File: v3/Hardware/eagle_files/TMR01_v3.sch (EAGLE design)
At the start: 28 parts, among them IC1 DS3231/SO, U1 ATMEGA328P_TQFP

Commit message: fixed sda scl in rtc
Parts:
- added TP3, TP4: TEST-POINT3X4, SparkFun-Connectors:TEST-POINT3X4
- S1: value MOMENTARY-SWITCH-SPST-SMD-5.2MM -> MOMENTARY-SWITCH-SPST; device SparkFun-Switches:MOMENTARY-SWITCH-SPST-SMD-5.2MM -> SparkFun-Switches:MOMENTARY-SWITCH-SPST
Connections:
- net RX: now also TP3.1
- net SCL: now also IC1.SCL, R2.1; no longer IC1.SDA, R3.1
- net SDA: now also IC1.SDA, R3.1; no longer IC1.SCL, R2.1
- net TX: now also TP4.1
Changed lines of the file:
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@@
 <part name="C1" library="Perfect_0402" deviceset="CAP_0402" device="" value="100nF"/>
 <part name="R5" library="Perfect_0402" deviceset="RES_0402" device="" value="10k"/>
-<part name="S1" library="SparkFun-Switches" deviceset="MOMENTARY-SWITCH-SPST" device="-SMD-5.2MM"/>
+<part name="S1" library="SparkFun-Switches" deviceset="MOMENTARY-SWITCH-SPST" device=""/>
+<part name="TP3" library="SparkFun-Connectors" deviceset="TEST-POINT" device="3X4"/>
+<part name="TP4" library="SparkFun-Connectors" deviceset="TEST-POINT" device="3X4"/>
 </parts>
 <sheets>
@@
 <instance part="S1" gate="G$1" x="83.82" y="124.46" smashed="yes">
 <attribute name="NAME" x="83.82" y="125.984" size="1.778" layer="95" font="vector" align="bottom-center"/>
+</instance>
+<instance part="TP3" gate="G$1" x="104.14" y="149.86" smashed="yes" rot="R180">
+<attribute name="NAME" x="106.68" y="149.86" size="1.778" layer="95" font="vector" rot="R180"/>
+</instance>
+<instance part="TP4" gate="G$1" x="104.14" y="144.78" smashed="yes" rot="R180">
+<attribute name="NAME" x="106.68" y="144.78" size="1.778" layer="95" font="vector" rot="R180"/>
 </instance>
 </instances>
@@
 <label x="182.88" y="139.7" size="1.778" layer="95"/>
 </segment>
+<segment>
+<wire x1="104.14" y1="149.86" x2="111.76" y2="149.86" width="0.1524" layer="91"/>
+<label x="109.22" y="149.86" size="1.778" layer="95"/>
+<pinref part="TP3" gate="G$1" pin="1"/>
+</segment>
 </net>
 <net name="TX" class="0">
@@
 <wire x1="177.8" y1="137.16" x2="185.42" y2="137.16" width="0.1524" layer="91"/>
 <label x="182.88" y="137.16" size="1.778" layer="95"/>
+</segment>
+<segment>
+<wire x1="104.14" y1="144.78" x2="111.76" y2="144.78" width="0.1524" layer="91"/>
+<label x="109.22" y="144.78" size="1.778" layer="95"/>
+<pinref part="TP4" gate="G$1" pin="1"/>
 </segment>
 </net>
@@
 </segment>
 <segment>
+<wire x1="170.18" y1="71.12" x2="187.96" y2="71.12" width="0.1524" layer="91"/>
+<wire x1="187.96" y1="71.12" x2="187.96" y2="78.74" width="0.1524" layer="91"/>
+<label x="172.72" y="71.12" size="1.778" layer="95"/>
+<pinref part="IC1" gate="G$1" pin="SDA"/>
+<pinref part="R3" gate="G$1" pin="1"/>
+</segment>
+</net>
+<net name="SCL" class="0">
+<segment>
+<pinref part="U1" gate="U1" pin="PC5(ADC5/SCL)"/>
+<wire x1="177.8" y1="149.86" x2="185.42" y2="149.86" width="0.1524" layer="91"/>
+<label x="182.88" y="149.86" size="1.778" layer="95"/>
+</segment>
+<segment>
 <pinref part="IC1" gate="G$1" pin="SCL"/>
 <wire x1="170.18" y1="73.66" x2="180.34" y2="73.66" width="0.1524" layer="91"/>
@@
 </segment>
 </net>
-<net name="SCL" class="0">
-<segment>
-<wire x1="170.18" y1="71.12" x2="187.96" y2="71.12" width="0.1524" layer="91"/>
-<wire x1="187.96" y1="71.12" x2="187.96" y2="78.74" width="0.1524" layer="91"/>
-<label x="172.72" y="71.12" size="1.778" layer="95"/>
-<pinref part="IC1" gate="G$1" pin="SDA"/>
-<pinref part="R3" gate="G$1" pin="1"/>
-</segment>
-<segment>
-<pinref part="U1" gate="U1" pin="PC5(ADC5/SCL)"/>
-<wire x1="177.8" y1="149.86" x2="185.42" y2="149.86" width="0.1524" layer="91"/>
-<label x="182.88" y="149.86" size="1.778" layer="95"/>
-</segment>
-</net>

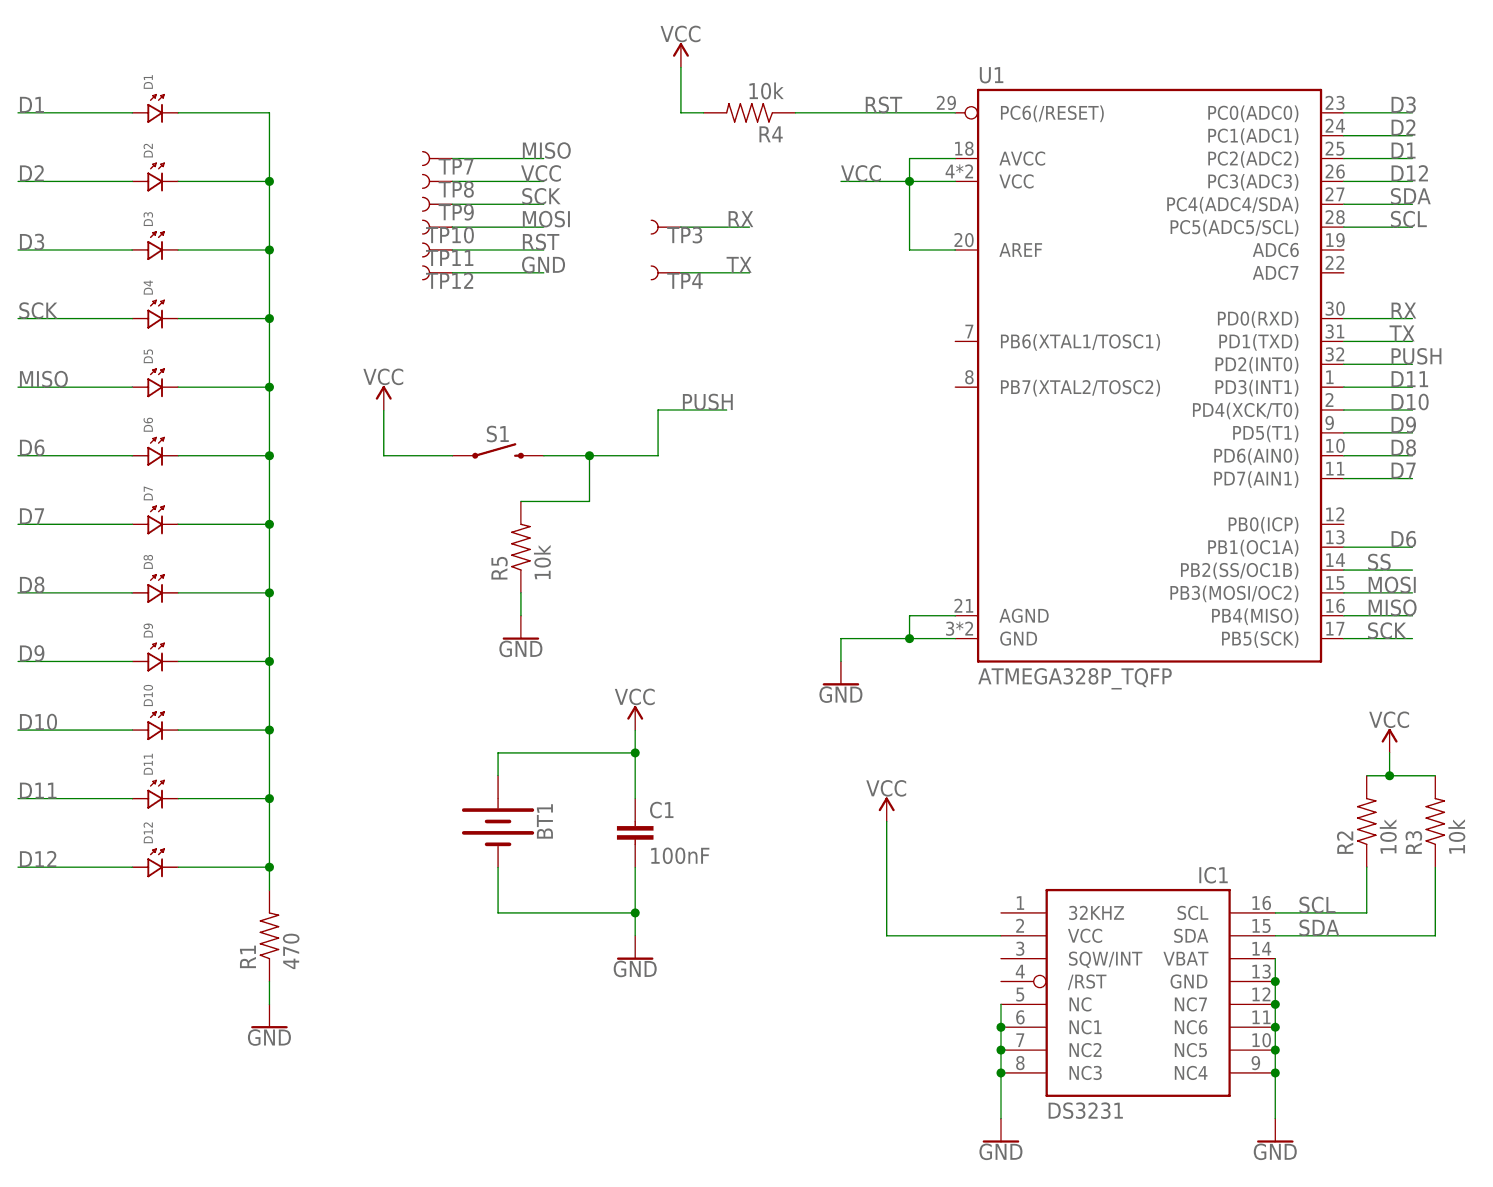
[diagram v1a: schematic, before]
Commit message: pins output modified, not using miso mosi connected to leds
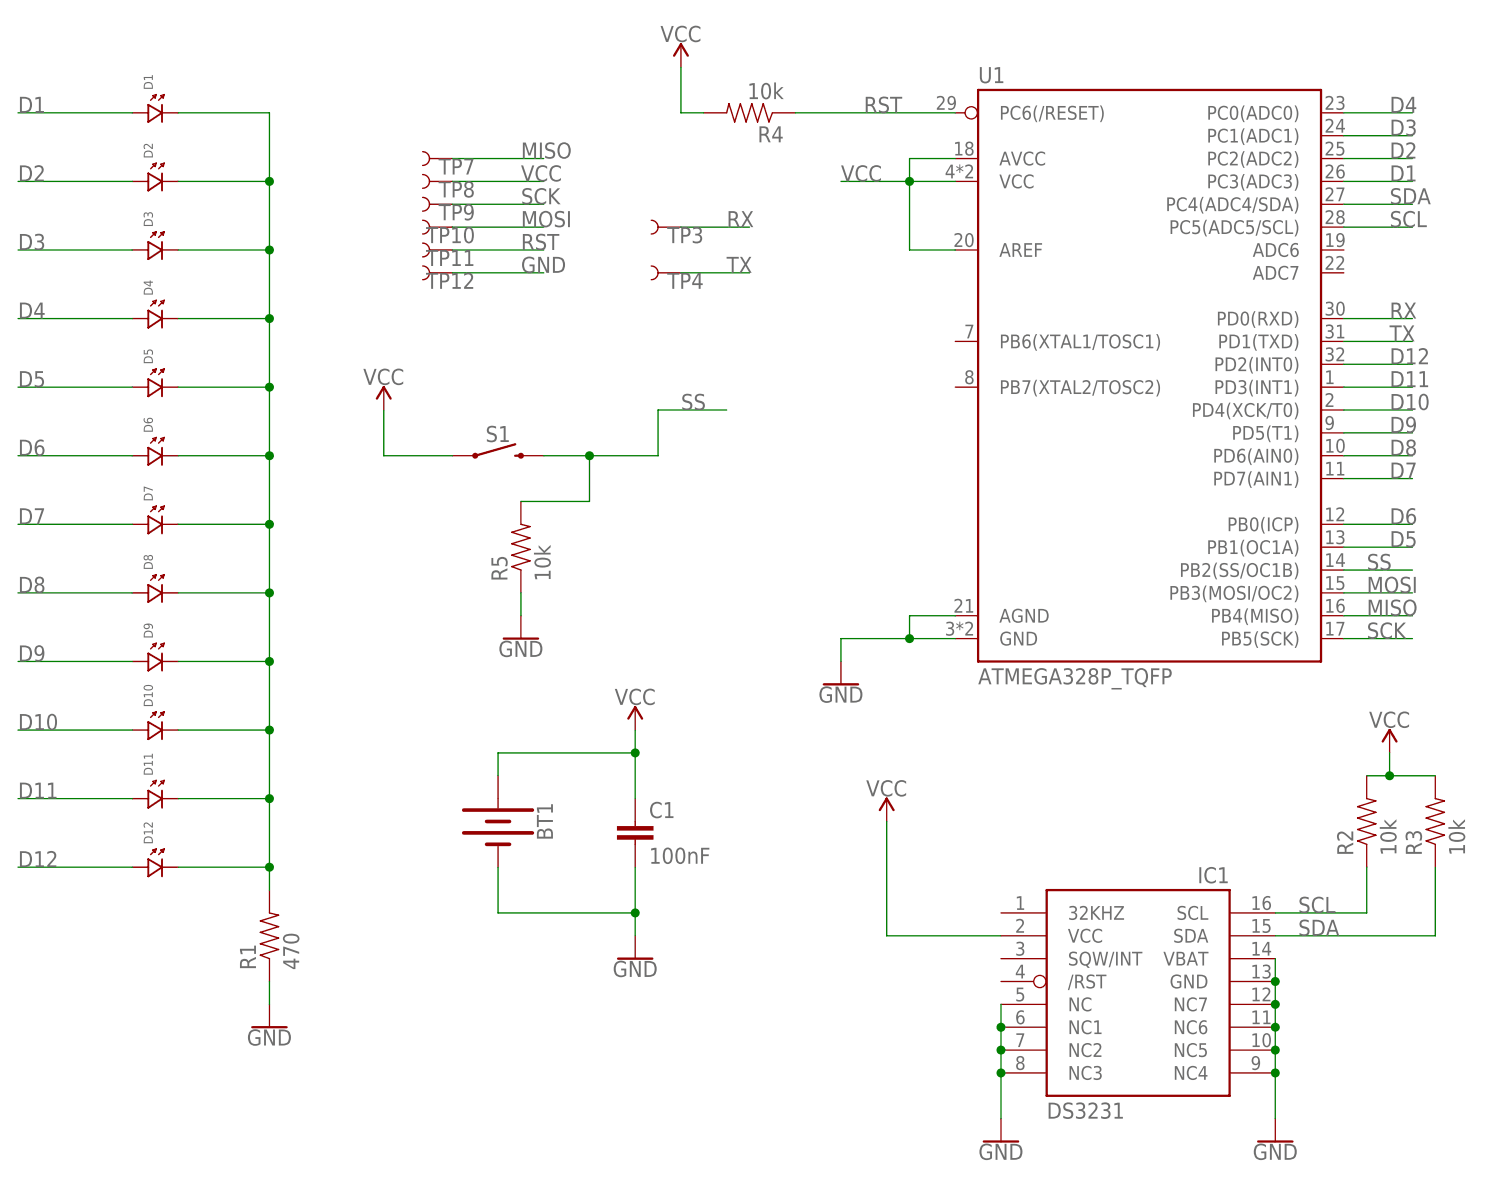
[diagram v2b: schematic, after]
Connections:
- removed net PUSH: R5.2, S1.2, U1.PD2(INT0)
- new net D4: D4.1, U1.PC0(ADC0)
- new net D5: D5.1, U1.PB1(OC1A)
- net D1: now also U1.PC3(ADC3); no longer U1.PC2(ADC2)
- net D12: now also U1.PD2(INT0); no longer U1.PC3(ADC3)
- net D2: now also U1.PC2(ADC2); no longer U1.PC1(ADC1)
- net D3: now also U1.PC1(ADC1); no longer U1.PC0(ADC0)
- net D6: now also U1.PB0(ICP); no longer U1.PB1(OC1A)
- net MISO: no longer D5.1
- net SCK: no longer D4.1
- net SS: now also R5.2, S1.2
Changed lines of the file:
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@@
 <pinref part="TP7" gate="G$1" pin="1"/>
-</segment>
-<segment>
-<wire x1="43.18" y1="132.08" x2="30.48" y2="132.08" width="0.1524" layer="91"/>
-<label x="30.48" y="132.08" size="1.778" layer="95"/>
-<pinref part="D5" gate="G$1" pin="1"/>
 </segment>
 </net>
@@
 <pinref part="TP9" gate="G$1" pin="1"/>
 </segment>
-<segment>
-<wire x1="43.18" y1="139.7" x2="30.48" y2="139.7" width="0.1524" layer="91"/>
-<label x="30.48" y="139.7" size="1.778" layer="95"/>
-<pinref part="D4" gate="G$1" pin="1"/>
-</segment>
 </net>
 <net name="D1" class="0">
@@
 </segment>
 <segment>
+<pinref part="U1" gate="U1" pin="PC3(ADC3)"/>
+<wire x1="177.8" y1="154.94" x2="185.42" y2="154.94" width="0.1524" layer="91"/>
+<label x="182.88" y="154.94" size="1.778" layer="95"/>
+</segment>
+</net>
+<net name="D2" class="0">
+<segment>
+<wire x1="43.18" y1="154.94" x2="30.48" y2="154.94" width="0.1524" layer="91"/>
+<label x="30.48" y="154.94" size="1.778" layer="95"/>
+<pinref part="D2" gate="G$1" pin="1"/>
+</segment>
+<segment>
 <pinref part="U1" gate="U1" pin="PC2(ADC2)"/>
 <wire x1="177.8" y1="157.48" x2="185.42" y2="157.48" width="0.1524" layer="91"/>
@@
 </segment>
 </net>
-<net name="D2" class="0">
-<segment>
-<wire x1="43.18" y1="154.94" x2="30.48" y2="154.94" width="0.1524" layer="91"/>
-<label x="30.48" y="154.94" size="1.778" layer="95"/>
-<pinref part="D2" gate="G$1" pin="1"/>
+<net name="D3" class="0">
+<segment>
+<wire x1="43.18" y1="147.32" x2="30.48" y2="147.32" width="0.1524" layer="91"/>
+<label x="30.48" y="147.32" size="1.778" layer="95"/>
+<pinref part="D3" gate="G$1" pin="1"/>
 </segment>
 <segment>
@@
 </segment>
 </net>
-<net name="D3" class="0">
-<segment>
-<wire x1="43.18" y1="147.32" x2="30.48" y2="147.32" width="0.1524" layer="91"/>
-<label x="30.48" y="147.32" size="1.778" layer="95"/>
-<pinref part="D3" gate="G$1" pin="1"/>
-</segment>
-<segment>
-<pinref part="U1" gate="U1" pin="PC0(ADC0)"/>
-<wire x1="177.8" y1="162.56" x2="185.42" y2="162.56" width="0.1524" layer="91"/>
-<label x="182.88" y="162.56" size="1.778" layer="95"/>
-</segment>
-</net>
 <net name="D6" class="0">
 <segment>
@@
 </segment>
 <segment>
-<pinref part="U1" gate="U1" pin="PB1(OC1A)"/>
-<wire x1="177.8" y1="114.3" x2="185.42" y2="114.3" width="0.1524" layer="91"/>
-<label x="182.88" y="114.3" size="1.778" layer="95"/>
-</segment>
-</net>
-<net name="PUSH" class="0">
+<pinref part="U1" gate="U1" pin="PB0(ICP)"/>
+<wire x1="177.8" y1="116.84" x2="185.42" y2="116.84" width="0.1524" layer="91"/>
+<label x="182.88" y="116.84" size="1.778" layer="95"/>
+</segment>
+</net>
+<net name="SS" class="0">
+<segment>
+<pinref part="U1" gate="U1" pin="PB2(SS/OC1B)"/>
+<wire x1="177.8" y1="111.76" x2="185.42" y2="111.76" width="0.1524" layer="91"/>
+<label x="180.34" y="111.76" size="1.778" layer="95"/>
+</segment>
 <segment>
 <wire x1="88.9" y1="124.46" x2="93.98" y2="124.46" width="0.1524" layer="91"/>
@@
 <pinref part="S1" gate="G$1" pin="2"/>
 </segment>
+</net>
+<net name="D12" class="0">
+<segment>
+<wire x1="43.18" y1="78.74" x2="30.48" y2="78.74" width="0.1524" layer="91"/>
+<label x="30.48" y="78.74" size="1.778" layer="95"/>
+<pinref part="D12" gate="G$1" pin="1"/>
+</segment>
 <segment>
 <pinref part="U1" gate="U1" pin="PD2(INT0)"/>
 <wire x1="177.8" y1="134.62" x2="185.42" y2="134.62" width="0.1524" layer="91"/>
 <label x="182.88" y="134.62" size="1.778" layer="95"/>
-</segment>
-</net>
-<net name="SS" class="0">
-<segment>
-<pinref part="U1" gate="U1" pin="PB2(SS/OC1B)"/>
-<wire x1="177.8" y1="111.76" x2="185.42" y2="111.76" width="0.1524" layer="91"/>
-<label x="180.34" y="111.76" size="1.778" layer="95"/>
-</segment>
-</net>
-<net name="D12" class="0">
-<segment>
-<pinref part="U1" gate="U1" pin="PC3(ADC3)"/>
-<wire x1="177.8" y1="154.94" x2="185.42" y2="154.94" width="0.1524" layer="91"/>
-<label x="182.88" y="154.94" size="1.778" layer="95"/>
-</segment>
-<segment>
-<wire x1="43.18" y1="78.74" x2="30.48" y2="78.74" width="0.1524" layer="91"/>
-<label x="30.48" y="78.74" size="1.778" layer="95"/>
-<pinref part="D12" gate="G$1" pin="1"/>
 </segment>
 </net>
@@
 </segment>
 </net>
+<net name="D5" class="0">
+<segment>
+<pinref part="U1" gate="U1" pin="PB1(OC1A)"/>
+<wire x1="177.8" y1="114.3" x2="185.42" y2="114.3" width="0.1524" layer="91"/>
+<label x="182.88" y="114.3" size="1.778" layer="95"/>
+</segment>
+<segment>
+<wire x1="43.18" y1="132.08" x2="30.48" y2="132.08" width="0.1524" layer="91"/>
+<label x="30.48" y="132.08" size="1.778" layer="95"/>
+<pinref part="D5" gate="G$1" pin="1"/>
+</segment>
+</net>
+<net name="D4" class="0">
+<segment>
+<pinref part="U1" gate="U1" pin="PC0(ADC0)"/>
+<wire x1="177.8" y1="162.56" x2="185.42" y2="162.56" width="0.1524" layer="91"/>
+<label x="182.88" y="162.56" size="1.778" layer="95"/>
+</segment>
+<segment>
+<wire x1="43.18" y1="139.7" x2="30.48" y2="139.7" width="0.1524" layer="91"/>
+<label x="30.48" y="139.7" size="1.778" layer="95"/>
+<pinref part="D4" gate="G$1" pin="1"/>
+</segment>
+</net>

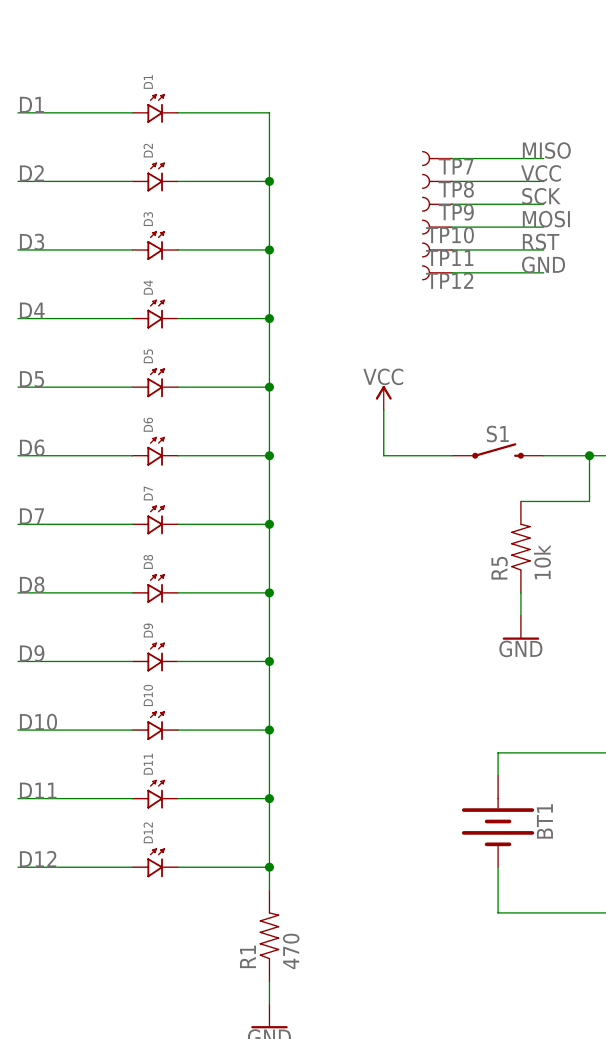
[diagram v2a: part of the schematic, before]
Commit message: 0402 leds possible wrong footprint. Changed temporaly by resistors footprint
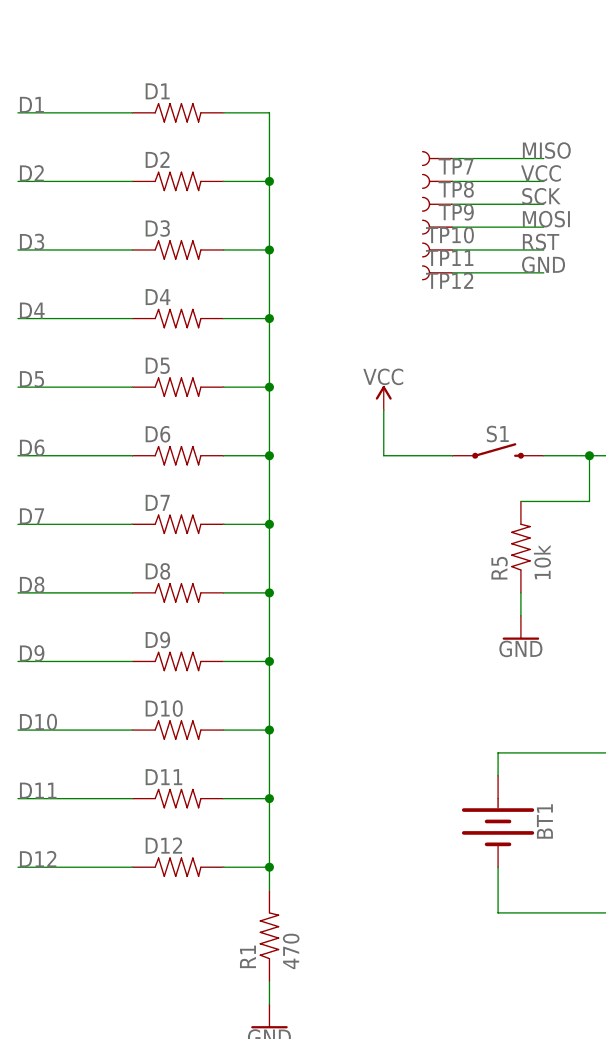
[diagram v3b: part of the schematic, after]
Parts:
- D1, D10, D11, D12, D2, D3, D4, D5, D6, D7, D8, D9: device standardparts:LED.0402 -> Perfect_0402:RES_0402
